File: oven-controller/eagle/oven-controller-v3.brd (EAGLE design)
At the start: 74.3 x 45.4 mm, 48 parts, among them Q1 FDV305N, Q2 FDV305N, Q3 FDV305N, Q4 FDV305N, U1 ARDUINO_SHIELDLONGPADS, U2 MAX31855, U3 MAX31855, U4 MAX31855, U5 MAX31855, U6 MAX31855

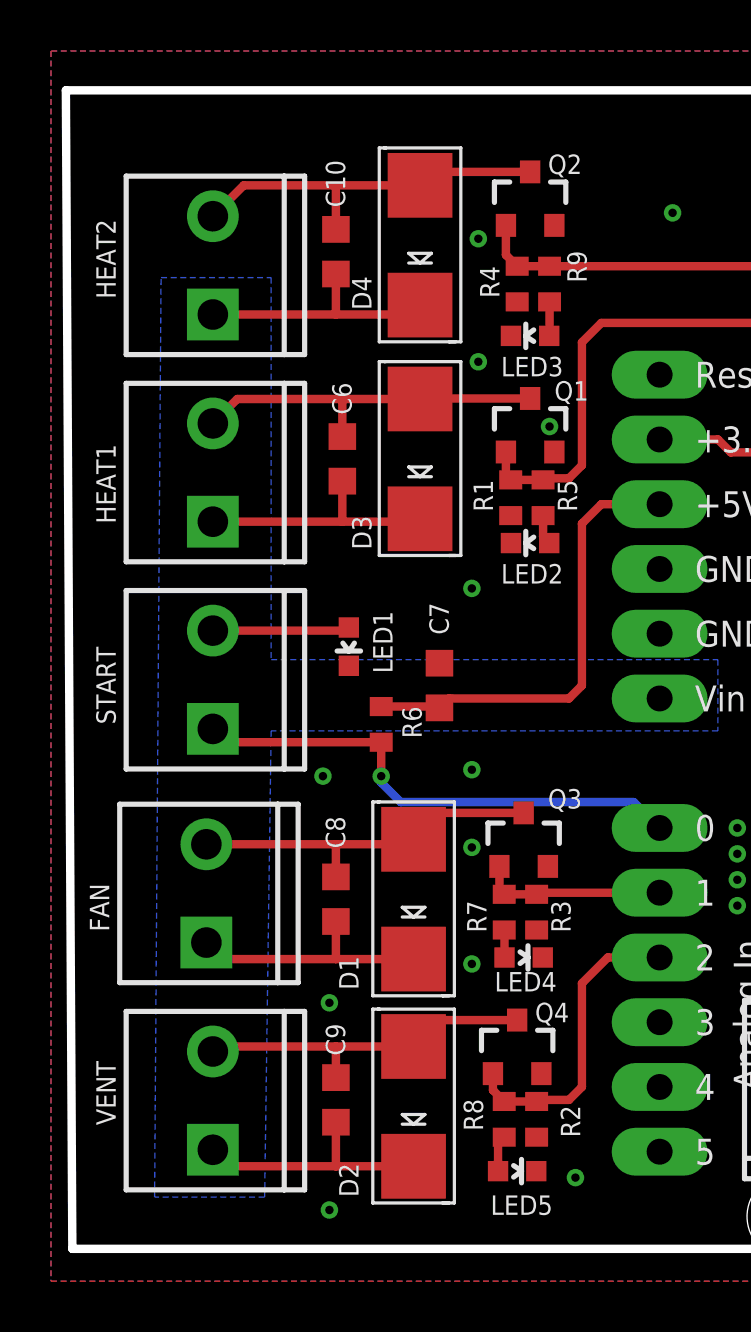
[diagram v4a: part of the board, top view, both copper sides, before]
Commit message: Fixed diode package.
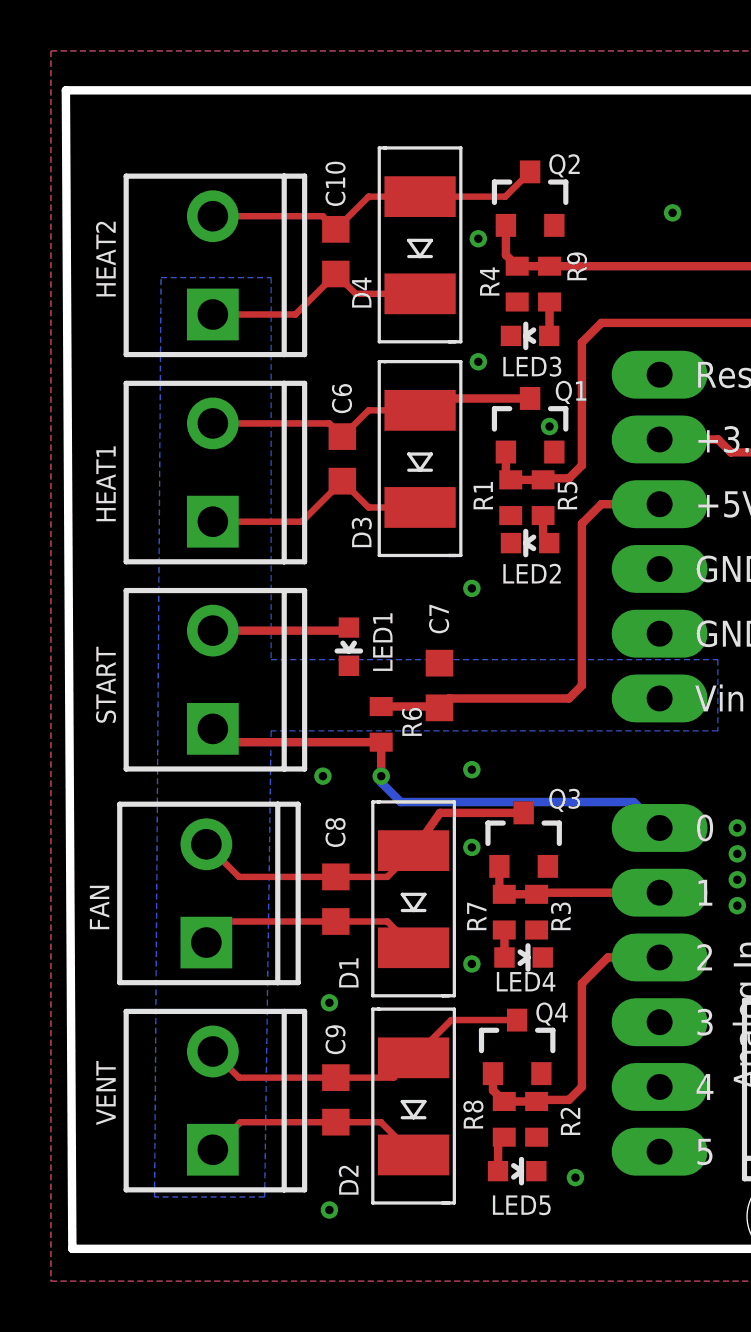
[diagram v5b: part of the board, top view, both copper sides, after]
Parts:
- D1, D2, D3, D4: device adafruit:SMADIODE -> wicker:DO-214AC-SMA
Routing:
- net 12V: track 39.4 -> 36.1 mm
- net N$21: track 14.9 -> 13.6 mm
- net N$3: track 14.4 -> 13.3 mm
- net N$4: track 14.3 -> 13.5 mm
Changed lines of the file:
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@@
 <attribute name="VALUE" x="16.478" y="3.01" size="1" layer="27" ratio="10" rot="R90"/>
 </element>
-<element name="D1" library="adafruit" package="SMADIODE" value="20V 1A" x="10.922" y="12.446" smashed="yes" rot="R90">
+<element name="D1" library="wicker" package="DO-214AC-SMA" value="20V 1A" x="10.922" y="12.446" smashed="yes" rot="R90">
 <attribute name="NAME" x="8.763" y="8.89" size="0.762" layer="25" font="vector" ratio="20" rot="R90"/>
 <attribute name="VALUE" x="13.208" y="9.906" size="0.4064" layer="27" font="vector" rot="R90"/>
 </element>
-<element name="D2" library="adafruit" package="SMADIODE" value="20V 1A" x="10.922" y="4.318" smashed="yes" rot="R90">
+<element name="D2" library="wicker" package="DO-214AC-SMA" value="20V 1A" x="10.922" y="4.318" smashed="yes" rot="R90">
 <attribute name="NAME" x="8.763" y="0.762" size="0.762" layer="25" font="vector" ratio="20" rot="R90"/>
 <attribute name="VALUE" x="13.208" y="1.778" size="0.4064" layer="27" font="vector" rot="R90"/>
 </element>
-<element name="D3" library="adafruit" package="SMADIODE" value="20V 1A" x="11.176" y="29.718" smashed="yes" rot="R90">
+<element name="D3" library="wicker" package="DO-214AC-SMA" value="20V 1A" x="11.176" y="29.718" smashed="yes" rot="R90">
 <attribute name="NAME" x="9.271" y="26.162" size="0.762" layer="25" font="vector" ratio="20" rot="R90"/>
 <attribute name="VALUE" x="13.462" y="27.178" size="0.4064" layer="27" font="vector" rot="R90"/>
 </element>
-<element name="D4" library="adafruit" package="SMADIODE" value="20V 1A" x="11.176" y="38.1" smashed="yes" rot="R90">
+<element name="D4" library="wicker" package="DO-214AC-SMA" value="20V 1A" x="11.176" y="38.1" smashed="yes" rot="R90">
 <attribute name="NAME" x="9.271" y="35.56" size="0.762" layer="25" font="vector" ratio="20" rot="R90"/>
 <attribute name="VALUE" x="13.462" y="35.56" size="0.4064" layer="27" font="vector" rot="R90"/>
@@
 <contactref element="VENT" pad="2"/>
 <contactref element="D2" pad="A"/>
-<wire x1="10.922" y1="6.6675" x2="7.874" y2="6.6675" width="0.3302" layer="1"/>
-<wire x1="7.874" y1="6.6675" x2="3.2437" y2="6.6675" width="0.3302" layer="1"/>
-<wire x1="3.2437" y1="6.6675" x2="3.048" y2="6.4718" width="0.3302" layer="1"/>
-<wire x1="11.4505" y1="7.196" x2="10.922" y2="6.6675" width="0.3302" layer="1"/>
-<wire x1="14.986" y1="7.704" x2="11.9585" y2="7.704" width="0.3302" layer="1"/>
-<wire x1="11.9585" y1="7.704" x2="10.922" y2="6.6675" width="0.3302" layer="1"/>
 <contactref element="C9" pad="1"/>
-<wire x1="7.874" y1="5.447" x2="7.874" y2="6.6675" width="0.3302" layer="1"/>
+<wire x1="7.874" y1="5.447" x2="4.0728" y2="5.447" width="0.254" layer="1"/>
+<wire x1="4.0728" y1="5.447" x2="3.048" y2="6.4718" width="0.254" layer="1"/>
+<wire x1="7.874" y1="5.447" x2="10.146" y2="5.447" width="0.254" layer="1"/>
+<wire x1="10.146" y1="5.447" x2="10.922" y2="6.223" width="0.254" layer="1"/>
+<wire x1="14.986" y1="7.704" x2="12.403" y2="7.704" width="0.254" layer="1"/>
+<wire x1="12.403" y1="7.704" x2="10.922" y2="6.223" width="0.254" layer="1"/>
 </signal>
 <signal name="CCO">
@@
 <contactref element="D3" pad="C"/>
 <contactref element="D4" pad="C"/>
-<wire x1="10.922" y1="1.9685" x2="7.874" y2="1.9685" width="0.3302" layer="1"/>
-<wire x1="7.874" y1="1.9685" x2="3.6957" y2="1.9685" width="0.3302" layer="1"/>
-<wire x1="3.6957" y1="1.9685" x2="3.048" y2="2.6162" width="0.3302" layer="1"/>
-<wire x1="3.048" y1="27.2542" x2="8.128" y2="27.2542" width="0.3302" layer="1"/>
-<wire x1="8.128" y1="27.2542" x2="11.0617" y2="27.2542" width="0.3302" layer="1"/>
-<wire x1="11.0617" y1="27.2542" x2="11.176" y2="27.3685" width="0.3302" layer="1"/>
-<wire x1="3.048" y1="35.3822" x2="7.874" y2="35.3822" width="0.3302" layer="1"/>
-<wire x1="7.874" y1="35.3822" x2="10.8077" y2="35.3822" width="0.3302" layer="1"/>
-<wire x1="10.8077" y1="35.3822" x2="11.176" y2="35.7505" width="0.3302" layer="1"/>
-<wire x1="10.922" y1="10.0965" x2="7.874" y2="10.0965" width="0.3302" layer="1"/>
-<wire x1="7.874" y1="10.0965" x2="3.4417" y2="10.0965" width="0.3302" layer="1"/>
-<wire x1="3.4417" y1="10.0965" x2="2.794" y2="10.7442" width="0.3302" layer="1"/>
 <contactref element="C9" pad="2"/>
 <contactref element="C8" pad="2"/>
 <contactref element="C6" pad="1"/>
 <contactref element="C10" pad="1"/>
-<wire x1="7.874" y1="36.971" x2="7.874" y2="35.3822" width="0.3302" layer="1"/>
-<wire x1="8.128" y1="28.843" x2="8.128" y2="27.2542" width="0.3302" layer="1"/>
-<wire x1="7.874" y1="3.697" x2="7.874" y2="1.9685" width="0.3302" layer="1"/>
-<wire x1="7.874" y1="11.571" x2="7.874" y2="10.0965" width="0.3302" layer="1"/>
+<wire x1="7.874" y1="3.697" x2="4.1288" y2="3.697" width="0.254" layer="1"/>
+<wire x1="4.1288" y1="3.697" x2="3.048" y2="2.6162" width="0.254" layer="1"/>
+<wire x1="7.874" y1="3.697" x2="9.638" y2="3.697" width="0.254" layer="1"/>
+<wire x1="9.638" y1="3.697" x2="10.922" y2="2.413" width="0.254" layer="1"/>
+<wire x1="7.874" y1="11.571" x2="3.6208" y2="11.571" width="0.254" layer="1"/>
+<wire x1="3.6208" y1="11.571" x2="2.794" y2="10.7442" width="0.254" layer="1"/>
+<wire x1="7.874" y1="11.571" x2="9.892" y2="11.571" width="0.254" layer="1"/>
+<wire x1="9.892" y1="11.571" x2="10.922" y2="10.541" width="0.254" layer="1"/>
+<wire x1="3.048" y1="27.2542" x2="6.5392" y2="27.2542" width="0.254" layer="1"/>
+<wire x1="6.5392" y1="27.2542" x2="8.128" y2="28.843" width="0.254" layer="1"/>
+<wire x1="11.176" y1="27.813" x2="9.158" y2="27.813" width="0.254" layer="1"/>
+<wire x1="9.158" y1="27.813" x2="8.128" y2="28.843" width="0.254" layer="1"/>
+<wire x1="11.176" y1="36.195" x2="8.65" y2="36.195" width="0.254" layer="1"/>
+<wire x1="8.65" y1="36.195" x2="7.874" y2="36.971" width="0.254" layer="1"/>
+<wire x1="3.048" y1="35.3822" x2="6.2852" y2="35.3822" width="0.254" layer="1"/>
+<wire x1="6.2852" y1="35.3822" x2="7.874" y2="36.971" width="0.254" layer="1"/>
 </signal>
 <signal name="N$7">
@@
 <contactref element="D3" pad="A"/>
 <wire x1="15.494" y1="32.088" x2="11.1965" y2="32.088" width="0.3302" layer="1"/>
-<wire x1="11.1965" y1="32.088" x2="11.176" y2="32.0675" width="0.3302" layer="1"/>
-<wire x1="11.176" y1="32.0675" x2="8.128" y2="32.0675" width="0.3302" layer="1"/>
-<wire x1="8.128" y1="32.0675" x2="4.0057" y2="32.0675" width="0.3302" layer="1"/>
-<wire x1="4.0057" y1="32.0675" x2="3.048" y2="31.1098" width="0.3302" layer="1"/>
+<wire x1="11.1965" y1="32.088" x2="11.176" y2="31.623" width="0.3302" layer="1"/>
 <contactref element="C6" pad="2"/>
-<wire x1="8.128" y1="30.593" x2="8.128" y2="32.0675" width="0.3302" layer="1"/>
+<wire x1="3.048" y1="31.1098" x2="7.6112" y2="31.1098" width="0.254" layer="1"/>
+<wire x1="7.6112" y1="31.1098" x2="8.128" y2="30.593" width="0.254" layer="1"/>
+<wire x1="11.176" y1="31.623" x2="9.158" y2="31.623" width="0.254" layer="1"/>
+<wire x1="9.158" y1="31.623" x2="8.128" y2="30.593" width="0.254" layer="1"/>
 </signal>
 <signal name="CS_HEAT1">
@@
 <contactref element="FAN" pad="2"/>
 <contactref element="D1" pad="A"/>
-<wire x1="2.794" y1="14.5998" x2="7.874" y2="14.5998" width="0.3302" layer="1"/>
-<wire x1="7.874" y1="14.5998" x2="10.7263" y2="14.5998" width="0.3302" layer="1"/>
-<wire x1="10.7263" y1="14.5998" x2="10.922" y2="14.7955" width="0.3302" layer="1"/>
 <wire x1="15.24" y1="15.832" x2="11.9585" y2="15.832" width="0.3302" layer="1"/>
-<wire x1="11.9585" y1="15.832" x2="10.922" y2="14.7955" width="0.3302" layer="1"/>
+<wire x1="11.9585" y1="15.832" x2="10.922" y2="14.351" width="0.3302" layer="1"/>
 <contactref element="C8" pad="1"/>
-<wire x1="7.874" y1="13.321" x2="7.874" y2="14.5998" width="0.3302" layer="1"/>
+<wire x1="7.874" y1="13.321" x2="9.892" y2="13.321" width="0.254" layer="1"/>
+<wire x1="9.892" y1="13.321" x2="10.922" y2="14.351" width="0.254" layer="1"/>
+<wire x1="7.874" y1="13.321" x2="4.0728" y2="13.321" width="0.254" layer="1"/>
+<wire x1="4.0728" y1="13.321" x2="2.794" y2="14.5998" width="0.254" layer="1"/>
 </signal>
 <signal name="CS_FAN">
@@
 <contactref element="HEAT2" pad="2"/>
 <contactref element="D4" pad="A"/>
-<wire x1="11.176" y1="40.4495" x2="7.874" y2="40.4495" width="0.3302" layer="1"/>
-<wire x1="7.874" y1="40.4495" x2="4.2597" y2="40.4495" width="0.3302" layer="1"/>
-<wire x1="4.2597" y1="40.4495" x2="3.048" y2="39.2378" width="0.3302" layer="1"/>
-<wire x1="15.494" y1="40.978" x2="11.7045" y2="40.978" width="0.3302" layer="1"/>
-<wire x1="11.7045" y1="40.978" x2="11.176" y2="40.4495" width="0.3302" layer="1"/>
 <contactref element="C10" pad="2"/>
-<wire x1="7.874" y1="38.721" x2="7.874" y2="40.4495" width="0.3302" layer="1"/>
+<wire x1="3.048" y1="39.2378" x2="7.3572" y2="39.2378" width="0.254" layer="1"/>
+<wire x1="7.3572" y1="39.2378" x2="7.874" y2="38.721" width="0.254" layer="1"/>
+<wire x1="11.176" y1="40.005" x2="9.158" y2="40.005" width="0.254" layer="1"/>
+<wire x1="9.158" y1="40.005" x2="7.874" y2="38.721" width="0.254" layer="1"/>
+<wire x1="11.176" y1="40.005" x2="14.521" y2="40.005" width="0.254" layer="1"/>
+<wire x1="14.521" y1="40.005" x2="15.494" y2="40.978" width="0.254" layer="1"/>
 </signal>
 <signal name="N$2">

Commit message: Lots of fixes. Reviewed. Passes ERC, DRC, rats. Ship it.
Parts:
- added C11, C12, C13, C14: 10n, rcl_custom:C0603K
- added R10: 1k, rcl_custom:0603-C-NOSILK
- C10, C6, C8, C9: value 100n -> 100n 100V
- C7: value 100n -> 10n
- FAN: value HDR4 -> (none); device SparkFun-Connectors:SCREWTERMINAL-3.5MM-2_LOCK -> con-phoenix-254:2POL254
- HEAT1: value HDR2 -> (none); device SparkFun-Connectors:SCREWTERMINAL-3.5MM-2_LOCK -> con-phoenix-254:2POL254
- HEAT2: value HDR3 -> (none); device SparkFun-Connectors:SCREWTERMINAL-3.5MM-2_LOCK -> con-phoenix-254:2POL254
- R5, R7, R8, R9: value 330 -> 1k
- R6: value 330 -> 10k
- START: value HDR1 -> (none); device SparkFun-Connectors:SCREWTERMINAL-3.5MM-2_LOCK -> con-phoenix-254:2POL254
- THERM1, THERM2, THERM3, THERM4, THERM5: device SparkFun-Connectors:SCREWTERMINAL-3.5MM-2_LOCK -> con-phoenix-254:2POL254
- U1: value ARDUINO_SHIELDLONGPADS -> ARDUINO_SHIELDNOHOLES; device SparkFun-Boards:DUEMILANOVE_SHIELD_LONGPADS -> SparkFun-Boards:DUEMILANOVE_SHIELD_NOHOLES
- VENT: value HDR5 -> (none); device SparkFun-Connectors:SCREWTERMINAL-3.5MM-2_LOCK -> con-phoenix-254:2POL254
- moved C7 52.0 mm to (62.7, 9.91), turned to 0 degrees
- moved THERM1 5.11 mm to (62.7, 5.59)
- moved HEAT2 4.58 mm to (4.57, 39.9), turned to 270 degrees
- moved THERM3 4.35 mm to (46.2, 5.59)
- moved THERM5 4.35 mm to (30.0, 5.59)
- moved THERM2 4.35 mm to (54.1, 5.59)
- moved THERM4 4.35 mm to (37.8, 5.59)
- moved HEAT1 4.10 mm to (4.57, 31.2), turned to 270 degrees
- moved FAN 4.02 mm to (5.08, 14.2)
- moved VENT 3.66 mm to (5.08, 5.84)
- moved Q4 3.41 mm to (18.0, 8.13)
- moved Q3 3.31 mm to (18.0, 16.5)
- moved R2 3.30 mm to (18.8, 5.08)
- moved U1 3.18 mm to (74.2, 58.7)
- moved U4 3.18 mm to (46.2, 15.0)
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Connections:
- net CS_FAN renamed FAN_EN
- net CS_HEAT1 renamed HEAT1_EN
- net CS_HEAT2 renamed HEAT2_EN
- net CS_VENT renamed VENT_EN
- net THERM_CS1 renamed THERM_!CS1
- net THERM_CS2 renamed THERM_!CS2
- net THERM_CS3 renamed THERM_!CS3
- net THERM_CS4 renamed THERM_!CS4
- net THERM_CS5 renamed THERM_!CS5
- removed net N$11: THERM2.2, U3.3
- removed net N$14: THERM4.1, U5.2
- removed net N$16: THERM5.1, U6.2
- removed net START: R6.1, START.1, U1.A0
- new net !START: LED1.C, R6.1, START.1, U1.A0
- new net N$1: LED1.A, R10.1
- new net N$10: C12.1, THERM3.1, U4.2
- new net N$20: C12.2, THERM3.2, U4.3
- net 12V: now also HEAT1.2, HEAT2.2; no longer HEAT1.1, HEAT2.1
- net 5V: now also R10.2; no longer C7.1
- net GND: now also START.2; no longer C7.2, LED1.C
- net N$12: now also C11.1, THERM2.1, U3.2; no longer THERM3.1, U4.2
- net N$13: now also C11.2, THERM2.2, U3.3; no longer THERM3.2, U4.3
- net N$15: now also C14.2, THERM5.2, U6.3; no longer THERM4.2, U5.3
- net N$17: now also C14.1, THERM5.1, U6.2; no longer THERM5.2, U6.3
- net N$2: now also C7.1, THERM1.1, U2.2; no longer LED1.A, START.2
- net N$21: now also HEAT2.1; no longer HEAT2.2
- net N$4: now also HEAT1.1; no longer HEAT1.2
- net N$5: now also C7.2, THERM1.2, U2.3; no longer THERM1.1, U2.2
- net N$6: now also C13.1, THERM4.1, U5.2; no longer THERM1.2, U2.3
- net N$8: now also C13.2, THERM4.2, U5.3; no longer THERM2.1, U3.2
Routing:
- net 12V: track 36.1 -> 0.00 mm
- net !START: track 0.00 -> 23.8 mm, vias 0 -> 1
- net START: track 20.1 -> 0.00 mm, vias 1 -> 0
- net HDR3: track 14.2 -> 0.00 mm
- net N$21: track 13.6 -> 0.00 mm
- net N$3: track 13.3 -> 0.00 mm
- net N$4: track 13.5 -> 4.76 mm
- net N$10: track 0.00 -> 6.97 mm
- net N$20: track 0.00 -> 6.97 mm
- net N$11: track 6.25 -> 0.00 mm
- net N$16: track 6.13 -> 0.00 mm
- net N$14: track 6.13 -> 0.00 mm
- net N$1: track 0.00 -> 2.56 mm
- net N$2: track 5.38 -> 7.23 mm
- net 5V: track 18.0 -> 19.7 mm
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- added copper zone on layer 1, net 12V
- added copper zone on layer 1, net HDR3
- added copper zone on layer 1, net N$21
- added copper zone on layer 1, net N$3
- added copper zone on layer 1, net N$4
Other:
- board size 74.3 x 45.4 mm -> 74.2 x 45.7 mm
